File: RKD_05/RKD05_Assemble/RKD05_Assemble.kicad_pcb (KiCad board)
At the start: 2 copper layers, 361.9 x 100 mm, 150 parts, among them J3 Conn_01x24, M1 Mark, M2 Mark, M3 Mark, M4 Mark, M5 Mark, M6 Mark, M7 Mark, SW1 SW_Push, SW10 SW_Push, SW11 SW_Push, SW12 SW_Push, SW13 SW_Push, SW14 SW_Push, SW15 SW_Push, SW16 SW_Push, SW17 SW_Push, SW18 SW_Push, SW19 SW_Push, SW2 SW_Push, SW20 SW_Push, SW21 SW_Push, SW22 SW_Push, SW23 SW_Push, SW24 SW_Push, SW25 SW_Push, SW26 SW_Push, SW27 SW_Push, SW28 SW_Push, SW29 SW_Push, SW3 SW_Push, SW30 SW_Push, SW4 SW_Push, SW40 RotaryEncoder_Switch, SW5 SW_Push, SW51 SW_Push, SW52 SW_Push, SW53 SW_Push, SW54 SW_Push, SW55 SW_Push, SW56 SW_Push, SW57 SW_Push, SW58 SW_Push, SW59 SW_Push, SW6 SW_Push, SW60 SW_Push, SW61 SW_Push, SW62 SW_Push, SW63 SW_Push, SW64 SW_Push, SW65 SW_Push, SW66 SW_Push, SW67 SW_Push, SW68 SW_Push, SW69 SW_Push, SW7 SW_Push, SW70 SW_Push, SW71 SW_Push, SW72 SW_Push, SW73 SW_Push, SW74 SW_Push, SW75 SW_Push, SW76 SW_Push, SW77 SW_Push, SW78 SW_Push, SW79 SW_Push, SW8 SW_Push, SW80 SW_Push, SW81 SW_Push, SW82 SW_Push, SW83 SW_Push, SW84 SW_Push, SW85 SW_Push, SW86 SW_Push, SW87 SW_Push, SW88 SW_Push, SW89 SW_Push, SW9 SW_Push, SW90 SW_Push

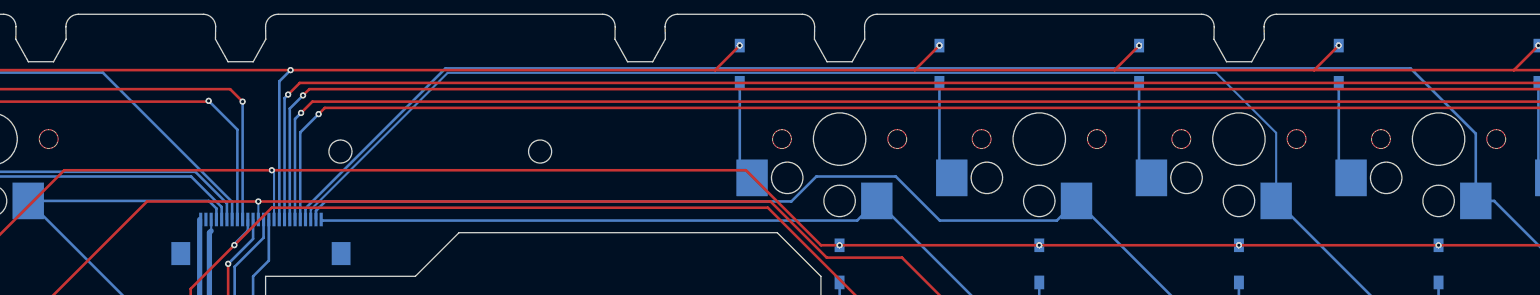
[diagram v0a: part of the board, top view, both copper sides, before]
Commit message: RKD05_width0.2配線を0.25に修正
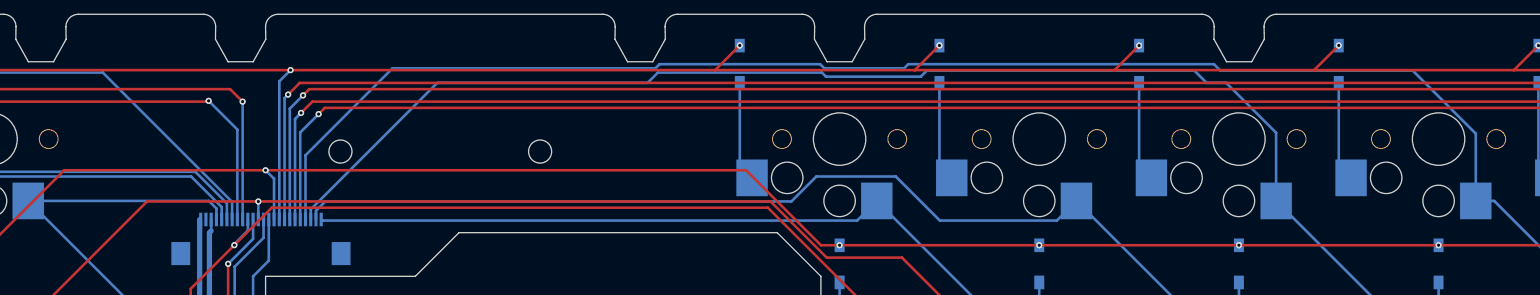
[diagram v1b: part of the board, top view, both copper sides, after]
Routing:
- net GP12:COL9: track 212.4 -> 216.0 mm
- net GP13:COL8: track 192.4 -> 192.9 mm
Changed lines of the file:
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@@
 		(tags "connector Hirose FH12 horizontal")
 		(property "Reference" "J3"
-			(at 0 3.7 360)
+			(at 0 3.7 0)
 			(layer "B.SilkS")
 			(effects
@@
 		)
 		(property "Value" "Conn_01x24"
-			(at 0 -5.6 360)
+			(at 0 -5.6 0)
 			(layer "B.Fab")
 			(effects
@@
 		)
 		(fp_text user "${REFERENCE}"
-			(at 0 -3.7 360)
+			(at 0 -3.7 0)
 			(layer "B.Fab")
 			(effects
@@
 	)
 	(segment
-		(start 149.590754 113.537592)
-		(end 149.590754 112.45)
-		(width 0.2)
+		(start 149.590754 112.45)
+		(end 149.590754 113.537592)
+		(width 0.25)
 		(layer "B.Cu")
 		(net 77)
@@
 	)
 	(segment
+		(start 270.25 110.675)
+		(end 270.25 104.259136)
+		(width 0.25)
+		(layer "B.Cu")
+		(net 81)
+	)
+	(segment
+		(start 158.590754 106.323531)
+		(end 158.590754 112.45)
+		(width 0.25)
+		(layer "B.Cu")
+		(net 81)
+	)
+	(segment
+		(start 215.704976 98.024975)
+		(end 208.091042 98.024975)
+		(width 0.25)
+		(layer "B.Cu")
+		(net 81)
+	)
+	(segment
 		(start 279.775 129.725)
 		(end 284.5375 134.4875)
@@
 	)
 	(segment
-		(start 158.590754 111.385836)
-		(end 158.590754 112.45)
+		(start 245.268956 97.631332)
+		(end 216.098619 97.631332)
+		(width 0.25)
+		(layer "B.Cu")
+		(net 81)
+	)
+	(segment
+		(start 191.977791 98.02508)
+		(end 166.889205 98.02508)
+		(width 0.25)
+		(layer "B.Cu")
+		(net 81)
+	)
+	(segment
+		(start 270.25 104.259136)
+		(end 264.217509 98.226645)
 		(width 0.25)
 		(layer "B.Cu")
@@
 	)
 	(segment
-		(start 270.25 110.675)
-		(end 270.25 104.259136)
+		(start 192.371539 97.631332)
+		(end 191.977791 98.02508)
 		(width 0.25)
 		(layer "B.Cu")
@@
 	)
 	(segment
+		(start 166.889205 98.02508)
+		(end 158.590754 106.323531)
+		(width 0.25)
+		(layer "B.Cu")
+		(net 81)
+	)
+	(segment
 		(start 284.5375 134.4875)
 		(end 284.5375 148.775)
@@
 	)
 	(segment
-		(start 264.022064 98.0312)
-		(end 171.94539 98.0312)
+		(start 245.864269 98.226645)
+		(end 245.268956 97.631332)
 		(width 0.25)
 		(layer "B.Cu")
@@
 	)
 	(segment
-		(start 270.25 104.259136)
-		(end 264.022064 98.0312)
+		(start 284.5375 148.775)
+		(end 289.3 153.5375)
 		(width 0.25)
 		(layer "B.Cu")
@@
 	)
 	(segment
-		(start 171.94539 98.0312)
-		(end 158.590754 111.385836)
+		(start 208.091042 98.024975)
+		(end 207.697399 97.631332)
 		(width 0.25)
 		(layer "B.Cu")
@@
 	)
 	(segment
-		(start 284.5375 148.775)
-		(end 289.3 153.5375)
+		(start 216.098619 97.631332)
+		(end 215.704976 98.024975)
 		(width 0.25)
 		(layer "B.Cu")
@@
 	)
 	(segment
+		(start 264.217509 98.226645)
+		(end 245.864269 98.226645)
+		(width 0.25)
+		(layer "B.Cu")
+		(net 81)
+	)
+	(segment
+		(start 207.697399 97.631332)
+		(end 192.371539 97.631332)
+		(width 0.25)
+		(layer "B.Cu")
+		(net 81)
+	)
+	(segment
 		(start 214.907632 108.346784)
 		(end 207.329866 108.346784)
@@
 	)
 	(segment
-		(start 260.725 120.2)
-		(end 260.725 129.725)
+		(start 159.090754 111.484604)
+		(end 171.158087 99.417271)
 		(width 0.25)
 		(layer "B.Cu")
@@
 	)
 	(segment
-		(start 159.090754 111.519959)
-		(end 172.154513 98.4562)
-		(width 0.2)
+		(start 171.158087 99.417271)
+		(end 191.221996 99.417271)
+		(width 0.25)
+		(layer "B.Cu")
+		(net 83)
+	)
+	(segment
+		(start 260.725 120.2)
+		(end 260.725 129.725)
+		(width 0.25)
 		(layer "B.Cu")
 		(net 83)
@@
 	)
 	(segment
-		(start 159.090754 112.45)
-		(end 159.090754 111.519959)
-		(width 0.2)
+		(start 192.208067 98.4312)
+		(end 207.860871 98.4312)
+		(width 0.25)
 		(layer "B.Cu")
 		(net 83)
@@
 	)
 	(segment
+		(start 191.221996 99.417271)
+		(end 192.208067 98.4312)
+		(width 0.25)
+		(layer "B.Cu")
+		(net 83)
+	)
+	(segment
+		(start 159.090754 112.45)
+		(end 159.090754 111.484604)
+		(width 0.25)
+		(layer "B.Cu")
+		(net 83)
+	)
+	(segment
+		(start 217.884558 98.226645)
+		(end 243.378357 98.226645)
+		(width 0.25)
+		(layer "B.Cu")
+		(net 83)
+	)
+	(segment
 		(start 260.725 129.725)
 		(end 265.4875 134.4875)
@@
 	)
 	(segment
-		(start 245.4766 98.4562)
+		(start 246.437671 99.417271)
 		(end 251.2 104.1796)
-		(width 0.2)
+		(width 0.25)
 		(layer "B.Cu")
 		(net 83)
@@
 	)
 	(segment
+		(start 207.860871 98.4312)
+		(end 208.251629 98.821958)
+		(width 0.25)
+		(layer "B.Cu")
+		(net 83)
+	)
+	(segment
+		(start 251.2 104.1796)
+		(end 251.2 110.675)
+		(width 0.25)
+		(layer "B.Cu")
+		(net 83)
+	)
+	(segment
+		(start 217.289245 98.821958)
+		(end 217.884558 98.226645)
+		(width 0.25)
+		(layer "B.Cu")
+		(net 83)
+	)
+	(segment
+		(start 208.251629 98.821958)
+		(end 217.289245 98.821958)
+		(width 0.25)
+		(layer "B.Cu")
+		(net 83)
+	)
+	(segment
 		(start 270.25 160.7125)
 		(end 270.25 167.825)
@@
 	)
 	(segment
-		(start 172.154513 98.4562)
-		(end 245.4766 98.4562)
-		(width 0.2)
+		(start 243.378357 98.226645)
+		(end 244.568983 99.417271)
+		(width 0.25)
 		(layer "B.Cu")
 		(net 83)
 	)
 	(segment
-		(start 251.2 104.1796)
-		(end 251.2 110.675)
-		(width 0.2)
+		(start 265.4875 148.775)
+		(end 265.4875 155.95)
+		(width 0.25)
 		(layer "B.Cu")
 		(net 83)
 	)
 	(segment
-		(start 265.4875 148.775)
-		(end 265.4875 155.95)
+		(start 244.568983 99.417271)
+		(end 246.437671 99.417271)
 		(width 0.25)
 		(layer "B.Cu")
@@
 	)
 	(segment
-		(start 155.376693 107.751653)
-		(end 200.620481 107.751653)
+		(start 128.5875 114.7312)
+		(end 128.5875 114.9062)
 		(width 0.25)
 		(layer "F.Cu")
@@
 	)
 	(segment
-		(start 28.575 114.9062)
-		(end 128.5875 114.9062)
+		(start 154.78138 107.751653)
+		(end 200.620481 107.751653)
 		(width 0.25)
 		(layer "F.Cu")
@@
 	)
 	(segment
-		(start 135.567047 107.751653)
-		(end 128.5875 114.7312)
+		(start 28.575 114.9062)
+		(end 128.5875 114.9062)
 		(width 0.25)
 		(layer "F.Cu")
@@
 	)
 	(segment
-		(start 200.620481 107.751653)
-		(end 207.775028 114.9062)
+		(start 154.78138 107.751653)
+		(end 135.567047 107.751653)
 		(width 0.25)
 		(layer "F.Cu")
@@
 	)
 	(segment
-		(start 155.376693 107.751653)
-		(end 135.567047 107.751653)
+		(start 347.6625 114.9062)
+		(end 209.55 114.9062)
 		(width 0.25)
 		(layer "F.Cu")
@@
 	)
 	(segment
-		(start 347.6625 114.9062)
-		(end 209.55 114.9062)
+		(start 200.620481 107.751653)
+		(end 207.775028 114.9062)
 		(width 0.25)
 		(layer "F.Cu")
@@
 	)
 	(segment
-		(start 128.5875 114.7312)
-		(end 128.5875 114.9062)
+		(start 135.567047 107.751653)
+		(end 128.5875 114.7312)
 		(width 0.25)
 		(layer "F.Cu")
@@
 	)
 	(via
-		(at 155.376693 107.751653)
+		(at 154.78138 107.751653)
 		(size 0.6)
 		(drill 0.3)
@@
 	)
 	(segment
-		(start 155.590754 107.965714)
-		(end 155.590754 112.45)
-		(width 0.2)
+		(start 154.78138 107.751653)
+		(end 155.590754 108.561027)
+		(width 0.25)
 		(layer "B.Cu")
 		(net 97)
 	)
 	(segment
-		(start 155.376693 107.751653)
-		(end 155.590754 107.965714)
-		(width 0.2)
+		(start 155.590754 108.561027)
+		(end 155.590754 112.45)
+		(width 0.25)
 		(layer "B.Cu")
 		(net 97)
@@
 		(start 154.090754 112.45)
 		(end 154.090754 110.728218)
-		(width 0.2)
+		(width 0.25)
 		(layer "B.Cu")
 		(net 98)

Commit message: RKD05　RE用PIN追加
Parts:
- added J1: Conn_01x02_Socket, Connector_PinHeader_2.54mm:PinHeader_1x02_P2.54mm_Horizontal, B.Cu at (159.8, 165.4)
- added M8: Mark, Rikkodo_FootPrint:rkd_LOGO_2x, F.Cu at (147.6, 104.8)
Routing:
- net RE1_A: track 0.00 -> 14.2 mm
- net RE1_B: track 0.00 -> 8.12 mm
- net GP08:COL13: track 317.3 -> 311.5 mm
- net GP23:COL0: track 220.9 -> 215.4 mm
- net GP09:COL12: track 284.3 -> 279.0 mm
- net GP10:COL11: track 254.3 -> 249.4 mm
- net GP11:COL10: track 233.1 -> 229.0 mm
- net GP24:COL1: track 203.8 -> 199.7 mm
- net GP17:ROW1: track 330.2 -> 326.6 mm
- net GP12:COL9: track 216.0 -> 213.0 mm
- net GP13:COL8: track 192.9 -> 190.5 mm
- net GP16:ROW0: track 366.1 -> 364.1 mm
- net GP22:ROW3: track 406.0 -> 406.8 mm
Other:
- outline, holes or cut-outs redrawn
- board text added: "RE_A"
- board text added: "RE_B"

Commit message: RKD05 ロゴの誤りを修正
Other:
- board text added: "RKD05_v1.0"
- board text removed: "RKD02_v1.0"
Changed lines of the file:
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@@
 		(tags "Through hole angled pin header THT 1x02 2.54mm single row")
 		(property "Reference" "J1"
-			(at 5.565626 1.701565 360)
+			(at 5.565626 1.701565 0)
 			(layer "B.SilkS")
 			(effects
@@
 		)
 		(property "Value" "Conn_01x02_Socket"
-			(at 4.385 -4.81 360)
+			(at 4.385 -4.81 0)
 			(layer "B.Fab")
 			(effects
@@
 		(layer "F.Fab")
 	)
-	(gr_text "RKD02_v1.0"
+	(gr_text "RKD05_v1.0"
 		(at 23.8125 178.59375 90)
 		(layer "B.SilkS")

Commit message: RKD05 GNDテキスト追加
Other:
- board text added: "3v3"
- board text added: "GND"
- board text added: "VCC"
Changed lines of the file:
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@@
 		(layer "F.Fab")
+	)
+	(gr_text "VCC"
+		(at 149.720968 108.64444 90)
+		(layer "B.SilkS")
+		(effects
+			(font
+				(size 1 1)
+				(thickness 0.1)
+			)
+			(justify left bottom mirror)
+		)
+	)
+	(gr_text "3v3"
+		(at 150.911592 108.64444 90)
+		(layer "B.SilkS")
+		(effects
+			(font
+				(size 1 1)
+				(thickness 0.1)
+			)
+			(justify left bottom mirror)
+		)
+	)
+	(gr_text "GND"
+		(at 148.530344 108.64444 90)
+		(layer "B.SilkS")
+		(effects
+			(font
+				(size 1 1)
+				(thickness 0.1)
+			)
+			(justify left bottom mirror)
+		)
 	)
 	(gr_text "RKD05_v1.0"

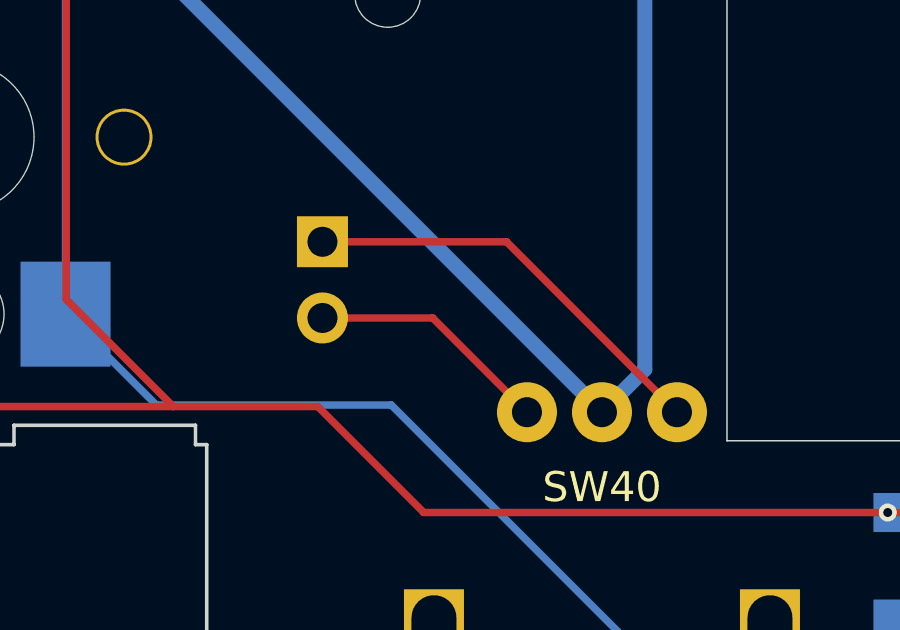
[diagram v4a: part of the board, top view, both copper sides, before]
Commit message: RKD05 PinAssign変更’
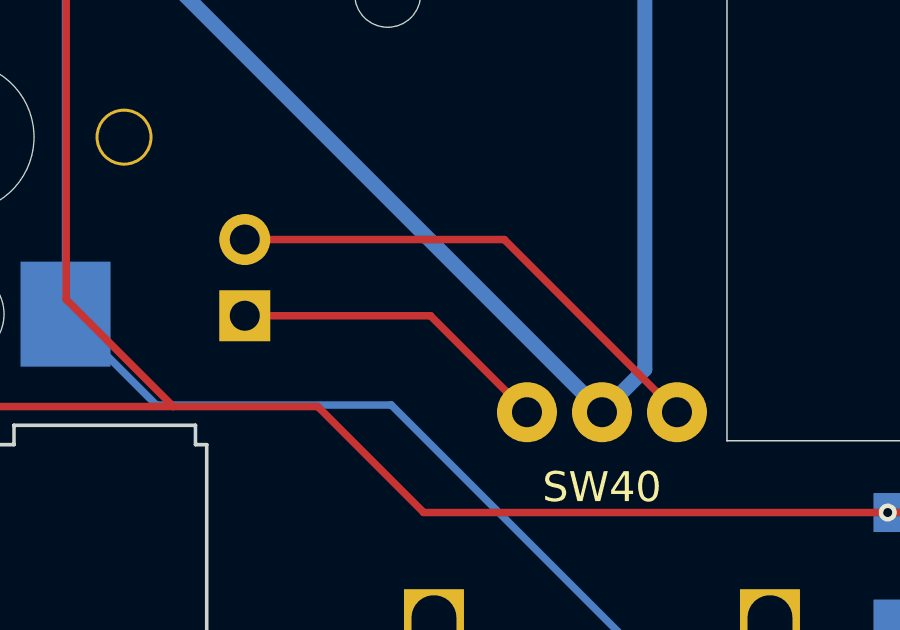
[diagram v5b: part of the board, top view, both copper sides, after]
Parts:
- moved J1 3.58 mm to (157.2, 167.9), turned to 0 degrees
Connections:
- J1 pad 1: RE1_A -> RE1_B
- J1 pad 2: RE1_B -> RE1_A
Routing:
- net RE1_A: track 14.2 -> 16.8 mm
- net RE1_B: track 8.12 -> 10.7 mm
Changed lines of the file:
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@@
 			)
 		)
+		(sheetname "ルート")
+		(sheetfile "RKD05_Assemble.kicad_sch")
 		(attr smd)
 		(fp_line
@@
 	(footprint "Connector_PinHeader_2.54mm:PinHeader_1x02_P2.54mm_Horizontal"
 		(layer "B.Cu")
-		(at 159.751693 165.41264 180)
+		(at 157.1625 167.878125)
 		(descr "Through hole angled pin header, 1x02, 2.54mm pitch, 6mm pin length, single row")
 		(tags "Through hole angled pin header THT 1x02 2.54mm single row")
@@
 		)
 		(property "Footprint" "Connector_PinHeader_2.54mm:PinHeader_1x02_P2.54mm_Horizontal"
-			(at 0 0 0)
+			(at 0 0 180)
 			(unlocked yes)
 			(layer "B.Fab")
@@
 		)
 		(property "Datasheet" ""
-			(at 0 0 0)
+			(at 0 0 180)
 			(unlocked yes)
 			(layer "B.Fab")
@@
 		)
 		(property "Description" "Generic connector, single row, 01x02, script generated (kicad-library-utils/schlib/autogen/connector/)"
-			(at 0 0 0)
+			(at 0 0 180)
 			(unlocked yes)
 			(layer "B.Fab")
@@
 		(attr through_hole)
 		(fp_line
-			(start 10.1 0.38)
-			(end 4.1 0.38)
+			(start -1.27 1.27)
+			(end -1.27 0)
 			(stroke
 				(width 0.12)
@@
 		)
 		(fp_line
-			(start 10.1 0.32)
-			(end 4.1 0.32)
+			(start 0 1.27)
+			(end -1.27 1.27)
 			(stroke
 				(width 0.12)
@@
 		)
 		(fp_line
-			(start 10.1 0.2)
-			(end 4.1 0.2)
+			(start 1.44 -3.87)
+			(end 1.44 1.33)
 			(stroke
 				(width 0.12)
@@
 		)
 		(fp_line
-			(start 10.1 0.08)
-			(end 4.1 0.08)
+			(start 1.44 -2.92)
+			(end 1.042929 -2.92)
 			(stroke
 				(width 0.12)
@@
 		)
 		(fp_line
-			(start 10.1 -0.04)
-			(end 4.1 -0.04)
+			(start 1.44 -2.16)
+			(end 1.042929 -2.16)
 			(stroke
 				(width 0.12)
@@
 		)
 		(fp_line
-			(start 10.1 -0.16)
-			(end 4.1 -0.16)
+			(start 1.44 -0.38)
+			(end 1.11 -0.38)
 			(stroke
 				(width 0.12)
@@
 		)
 		(fp_line
-			(start 10.1 -0.28)
-			(end 4.1 -0.28)
+			(start 1.44 0.38)
+			(end 1.11 0.38)
 			(stroke
 				(width 0.12)
@@
 		)
 		(fp_line
-			(start 10.1 -0.38)
-			(end 10.1 0.38)
+			(start 1.44 1.33)
+			(end 4.1 1.33)
 			(stroke
 				(width 0.12)
@@
 		)
 		(fp_line
-			(start 10.1 -2.16)
-			(end 4.1 -2.16)
+			(start 4.1 -3.87)
+			(end 1.44 -3.87)
 			(stroke
 				(width 0.12)
@@
 		)
 		(fp_line
-			(start 10.1 -2.92)
-			(end 10.1 -2.16)
+			(start 4.1 -2.92)
+			(end 10.1 -2.92)
 			(stroke
 				(width 0.12)
@@
 		)
 		(fp_line
-			(start 4.1 1.33)
-			(end 4.1 -3.87)
+			(start 4.1 -1.27)
+			(end 1.44 -1.27)
 			(stroke
 				(width 0.12)
@@
 		)
 		(fp_line
-			(start 4.1 -1.27)
-			(end 1.44 -1.27)
+			(start 4.1 1.33)
+			(end 4.1 -3.87)
 			(stroke
 				(width 0.12)
@@
 		)
 		(fp_line
-			(start 4.1 -2.92)
-			(end 10.1 -2.92)
+			(start 10.1 -2.92)
+			(end 10.1 -2.16)
 			(stroke
 				(width 0.12)
@@
 		)
 		(fp_line
-			(start 4.1 -3.87)
-			(end 1.44 -3.87)
+			(start 10.1 -2.16)
+			(end 4.1 -2.16)
 			(stroke
 				(width 0.12)
@@
 		)
 		(fp_line
-			(start 1.44 1.33)
-			(end 4.1 1.33)
+			(start 10.1 -0.38)
+			(end 10.1 0.38)
 			(stroke
 				(width 0.12)
@@
 		)
 		(fp_line
-			(start 1.44 0.38)
-			(end 1.11 0.38)
+			(start 10.1 -0.28)
+			(end 4.1 -0.28)
 			(stroke
 				(width 0.12)
@@
 		)
 		(fp_line
-			(start 1.44 -0.38)
-			(end 1.11 -0.38)
+			(start 10.1 -0.16)
+			(end 4.1 -0.16)
 			(stroke
 				(width 0.12)
@@
 		)
 		(fp_line
-			(start 1.44 -2.16)
-			(end 1.042929 -2.16)
+			(start 10.1 -0.04)
+			(end 4.1 -0.04)
 			(stroke
 				(width 0.12)
@@
 		)
 		(fp_line
-			(start 1.44 -2.92)
-			(end 1.042929 -2.92)
+			(start 10.1 0.08)
+			(end 4.1 0.08)
 			(stroke
 				(width 0.12)
@@
 		)
 		(fp_line
-			(start 1.44 -3.87)
-			(end 1.44 1.33)
+			(start 10.1 0.2)
+			(end 4.1 0.2)
 			(stroke
 				(width 0.12)
@@
 		)
 		(fp_line
-			(start 0 1.27)
-			(end -1.27 1.27)
+			(start 10.1 0.32)
+			(end 4.1 0.32)
 			(stroke
 				(width 0.12)
@@
 		)
 		(fp_line
-			(start -1.27 1.27)
-			(end -1.27 0)
+			(start 10.1 0.38)
+			(end 4.1 0.38)
 			(stroke
 				(width 0.12)
@@
 		)
 		(fp_line
-			(start 10.55 1.8)
-			(end 10.55 -4.35)
+			(start -1.8 -4.35)
+			(end -1.8 1.8)
 			(stroke
 				(width 0.05)
@@
 		)
 		(fp_line
-			(start 10.55 -4.35)
-			(end -1.8 -4.35)
+			(start -1.8 1.8)
+			(end 10.55 1.8)
 			(stroke
 				(width 0.05)
@@
 		)
 		(fp_line
-			(start -1.8 1.8)
-			(end 10.55 1.8)
+			(start 10.55 -4.35)
+			(end -1.8 -4.35)
 			(stroke
 				(width 0.05)
@@
 		)
 		(fp_line
-			(start -1.8 -4.35)
-			(end -1.8 1.8)
+			(start 10.55 1.8)
+			(end 10.55 -4.35)
 			(stroke
 				(width 0.05)
@@
 		)
 		(fp_line
-			(start 10.04 0.32)
-			(end 4.04 0.32)
+			(start -0.32 -2.86)
+			(end -0.32 -2.22)
 			(stroke
 				(width 0.1)
@@
 		)
 		(fp_line
-			(start 10.04 -0.32)
-			(end 10.04 0.32)
+			(start -0.32 -0.32)
+			(end -0.32 0.32)
 			(stroke
 				(width 0.1)
@@
 		)
 		(fp_line
-			(start 10.04 -0.32)
-			(end 4.04 -0.32)
+			(start 1.5 -3.81)
+			(end 4.04 -3.81)
 			(stroke
 				(width 0.1)
@@
 		)
 		(fp_line
-			(start 10.04 -2.22)
-			(end 4.04 -2.22)
+			(start 1.5 -2.86)
+			(end -0.32 -2.86)
 			(stroke
 				(width 0.1)
@@
 		)
 		(fp_line
-			(start 10.04 -2.86)
-			(end 10.04 -2.22)
+			(start 1.5 -2.22)
+			(end -0.32 -2.22)
 			(stroke
 				(width 0.1)
@@
 		)
 		(fp_line
-			(start 10.04 -2.86)
-			(end 4.04 -2.86)
+			(start 1.5 -0.32)
+			(end -0.32 -0.32)
 			(stroke
 				(width 0.1)
@@
 		)
 		(fp_line
-			(start 4.04 1.27)
-			(end 2.135 1.27)
+			(start 1.5 0.32)
+			(end -0.32 0.32)
 			(stroke
 				(width 0.1)
@@
 		)
 		(fp_line
-			(start 4.04 -3.81)
-			(end 4.04 1.27)
+			(start 1.5 0.635)
+			(end 1.5 -3.81)
 			(stroke
 				(width 0.1)
@@
 		)
 		(fp_line
-			(start 1.5 0.635)
-			(end 1.5 -3.81)
+			(start 4.04 -3.81)
+			(end 4.04 1.27)
 			(stroke
 				(width 0.1)
@@
 		)
 		(fp_line
-			(start 1.5 0.32)
-			(end -0.32 0.32)
+			(start 4.04 1.27)
+			(end 2.135 1.27)
 			(stroke
 				(width 0.1)
@@
 		)
 		(fp_line
-			(start 1.5 -0.32)
-			(end -0.32 -0.32)
+			(start 10.04 -2.86)
+			(end 4.04 -2.86)
 			(stroke
 				(width 0.1)
@@
 		)
 		(fp_line
-			(start 1.5 -2.22)
-			(end -0.32 -2.22)
+			(start 10.04 -2.86)
+			(end 10.04 -2.22)
 			(stroke
 				(width 0.1)
@@
 		)
 		(fp_line
-			(start 1.5 -2.86)
-			(end -0.32 -2.86)
+			(start 10.04 -2.22)
+			(end 4.04 -2.22)
 			(stroke
 				(width 0.1)
@@
 		)
 		(fp_line
-			(start 1.5 -3.81)
-			(end 4.04 -3.81)
+			(start 10.04 -0.32)
+			(end 4.04 -0.32)
 			(stroke
 				(width 0.1)
@@
 		)
 		(fp_line
-			(start -0.32 -0.32)
-			(end -0.32 0.32)
+			(start 10.04 -0.32)
+			(end 10.04 0.32)
 			(stroke
 				(width 0.1)
@@
 		)
 		(fp_line
-			(start -0.32 -2.86)
-			(end -0.32 -2.22)
+			(start 10.04 0.32)
+			(end 4.04 0.32)
 			(stroke
 				(width 0.1)
@@
 		)
 		(pad "1" thru_hole rect
-			(at 0 0 180)
+			(at 0 0)
 			(size 1.7 1.7)
 			(drill 1)
@@
 			)
 			(remove_unused_layers no)
-			(net 73 "RE1_A")
+			(net 74 "RE1_B")
 			(pinfunction "Pin_1")
 			(pintype "passive")
 		)
 		(pad "2" thru_hole oval
-			(at 0 -2.54 180)
+			(at 0 -2.54)
 			(size 1.7 1.7)
 			(drill 1)
@@
 			)
 			(remove_unused_layers no)
-			(net 74 "RE1_B")
+			(net 73 "RE1_A")
 			(pinfunction "Pin_2")
 			(pintype "passive")
@@
 	)
 	(segment
-		(start 165.88764 165.41264)
-		(end 159.751693 165.41264)
+		(start 165.813125 165.338125)
+		(end 157.1625 165.338125)
 		(width 0.25)
 		(layer "F.Cu")
@@
 	(segment
 		(start 171.56875 171.09375)
-		(end 165.88764 165.41264)
+		(end 165.813125 165.338125)
 		(width 0.25)
 		(layer "F.Cu")
@@
 	)
 	(segment
-		(start 159.751693 167.95264)
-		(end 163.42764 167.95264)
+		(start 163.353125 167.878125)
+		(end 166.56875 171.09375)
 		(width 0.25)
 		(layer "F.Cu")
@@
 	)
 	(segment
-		(start 163.42764 167.95264)
-		(end 166.56875 171.09375)
+		(start 157.1625 167.878125)
+		(end 163.353125 167.878125)
 		(width 0.25)
 		(layer "F.Cu")
